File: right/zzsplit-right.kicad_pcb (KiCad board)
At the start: 2 copper layers, 160.9 x 98.9 mm, 77 parts, among them J1 OLED, J2 MJ-4PP-9-Lily58-cache, J3 OLED, SW1 SW_PUSH-MX_W_LED, SW10 SW_PUSH-MX_W_LED, SW11 SW_PUSH-MX_W_LED, SW12 SW_PUSH-MX_W_LED, SW13 SW_PUSH-MX_W_LED, SW14 SW_PUSH-MX_W_LED, SW15 SW_PUSH-MX_W_LED, SW16 SW_PUSH-MX_W_LED, SW17 SW_PUSH-MX_W_LED, SW18 SW_PUSH-MX_W_LED, SW19 SW_PUSH-MX_W_LED, SW2 SW_PUSH-MX_W_LED, SW20 SW_PUSH-MX_W_LED, SW21 SW_PUSH-MX_W_LED, SW22 SW_PUSH-MX_W_LED, SW23 SW_PUSH-MX_W_LED, SW24 SW_PUSH-MX_W_LED, SW25 SW_PUSH-MX_W_LED, SW26 SW_PUSH-MX_W_LED, SW27 SW_PUSH-MX_W_LED, SW28 SW_PUSH-MX_W_LED, SW29 SW_PUSH-MX_W_LED, SW3 SW_PUSH-MX_W_LED, SW30 SW_PUSH-MX_W_LED, SW31 SW_SPDT, SW32 SW_Push, SW4 SW_PUSH-MX_W_LED, SW5 SW_PUSH-MX_W_LED, SW6 SW_PUSH-MX_W_LED, SW7 SW_PUSH-MX_W_LED, SW8 SW_PUSH-MX_W_LED, SW9 SW_PUSH-MX_W_LED, U1 ProMicro

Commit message: pcb fixup && new gerber
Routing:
- net GND: track 198.5 -> 209.7 mm, vias 42 -> 52
- net VDD: track 1395.2 -> 1401.0 mm
- net Net-(SW16-Pad3): track 45.3 -> 43.9 mm
- net Col4: track 180.0 -> 181.1 mm

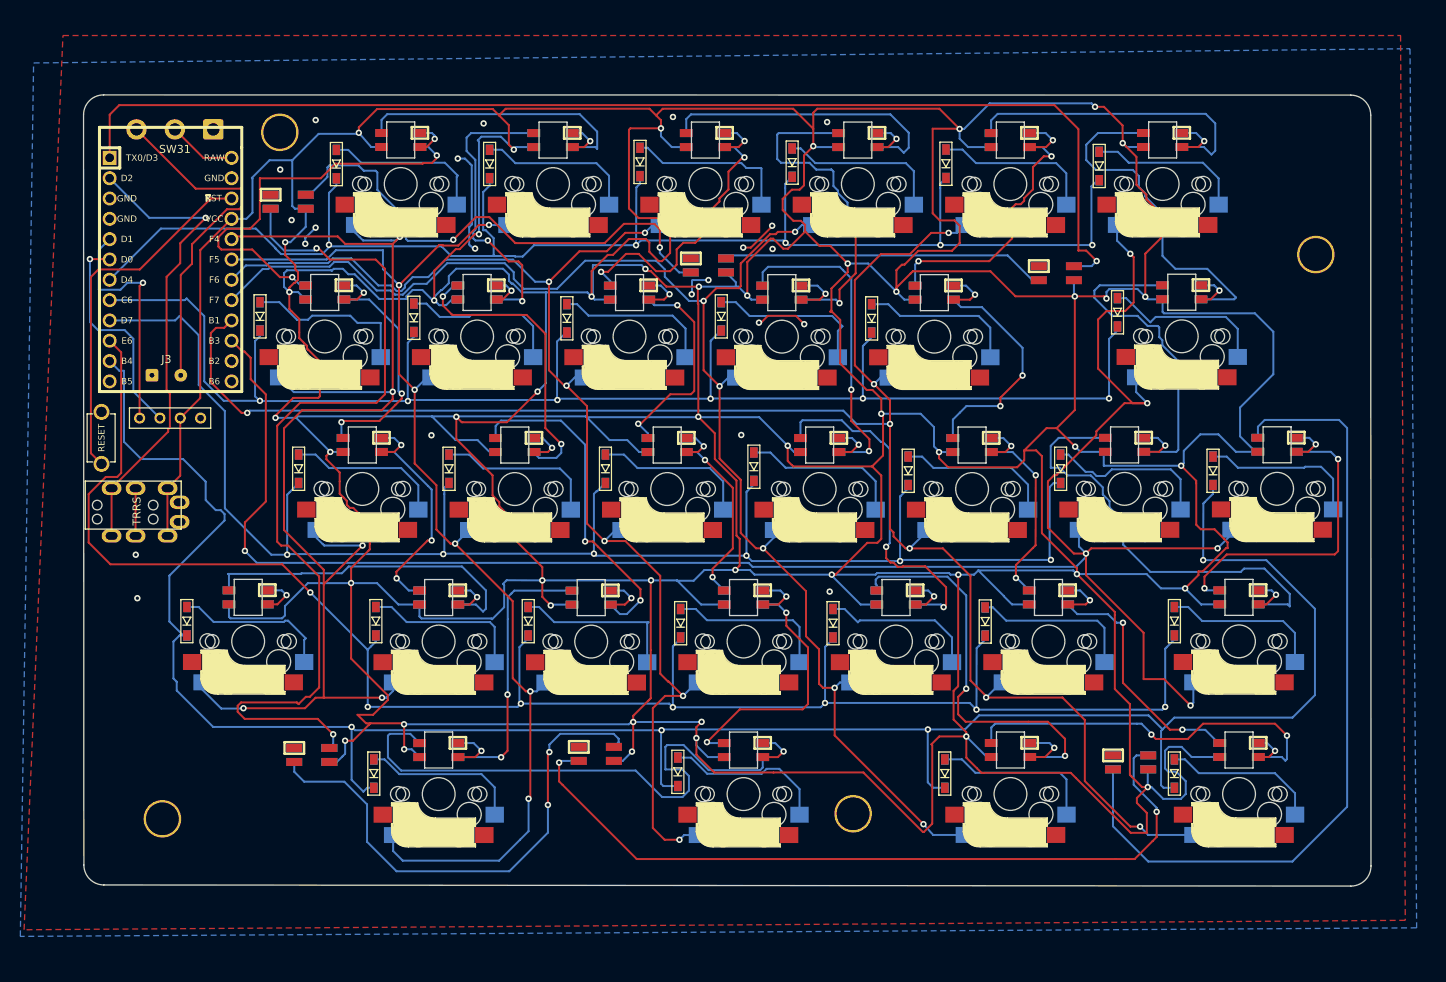
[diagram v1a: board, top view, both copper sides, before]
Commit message: fix rgb powerline problem and new 3 pin 2 channel switches
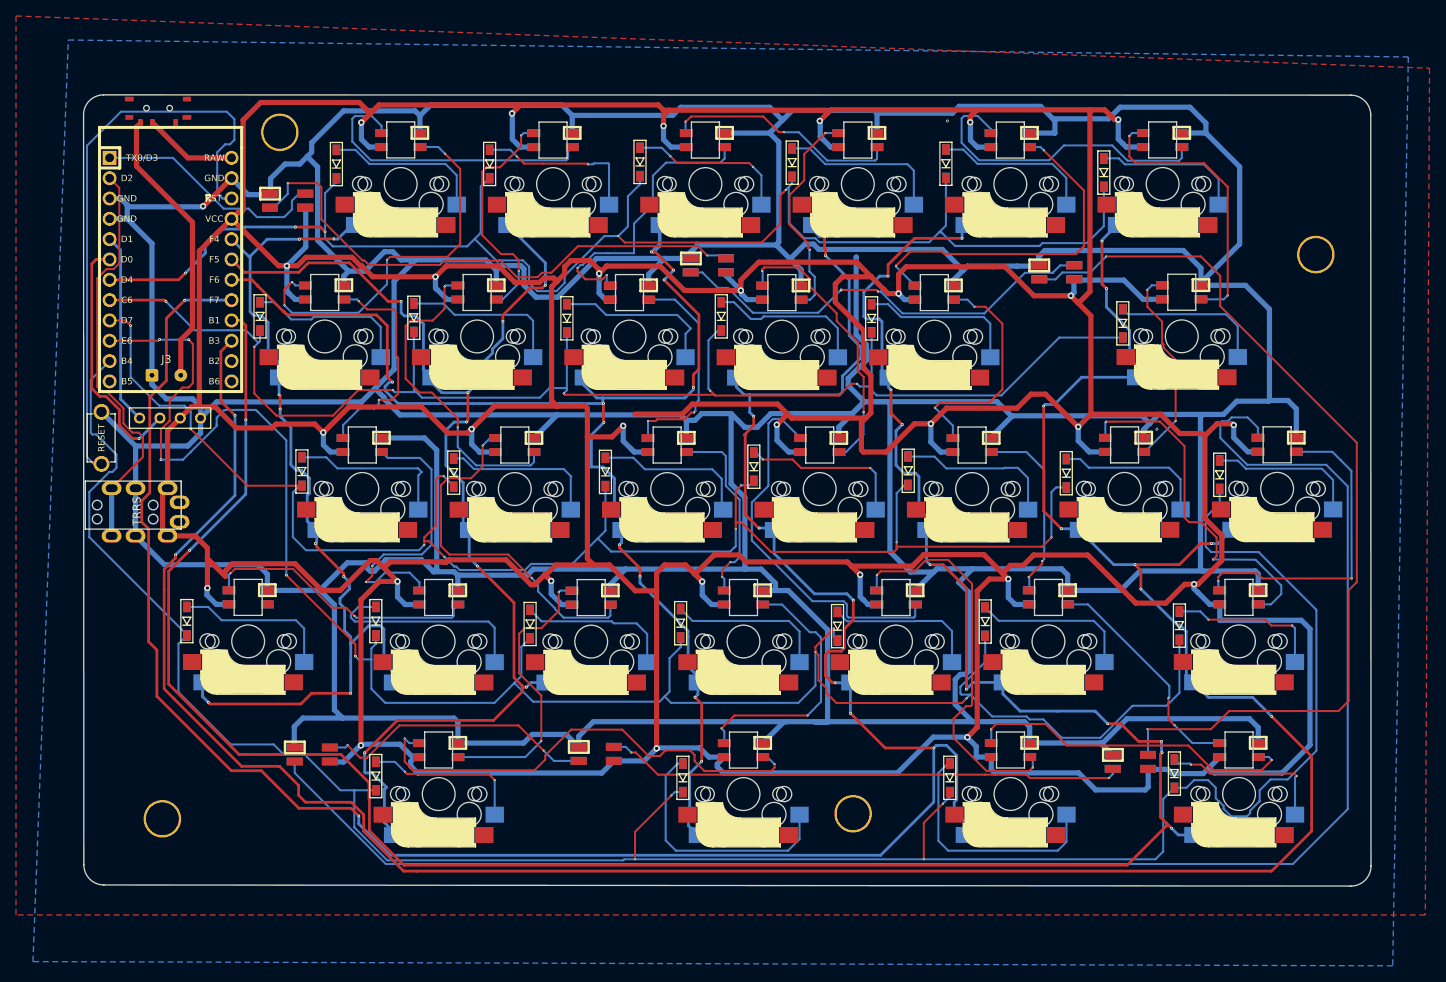
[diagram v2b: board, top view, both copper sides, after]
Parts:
- J3: value OLED -> Conn_01x02_Female
- SW31: footprint Connector_Wire:SolderWire-0.75sqmm_1x03_P4.8mm_D1.25mm_OD2.3mm -> switch:switch-MSK-12C02-smd
- moved D34 102.3 mm to (218.8, 130.4)
- moved D36 102.3 mm to (116.5, 129.4)
- moved D31 96.5 mm to (113.4, 60.2)
- moved D33 96.5 mm to (209.6, 69.2)
- moved SW31 7.98 mm to (97.2, 47.3), turned to -90 degrees
- moved D27 1.53 mm to (217.8, 75.5)
- moved D26 1.00 mm to (215.5, 56.7)
- moved D15 0.98 mm to (162.8, 132.4)
- moved D30 0.97 mm to (229.9, 94.5)
- moved D28 0.90 mm to (210.8, 94.3)
- moved D29 0.84 mm to (224.9, 113.3)
- moved D20 0.82 mm to (196.2, 132.4)
- moved D8 0.76 mm to (134.2, 94.2)
- moved D19 0.67 mm to (182.2, 113.4)
- moved D3 0.54 mm to (115.2, 94.1)
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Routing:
- net GND: track 209.7 -> 1098.1 mm, vias 52 -> 3
- net VDD: track 1401.0 -> 1122.2 mm, vias 48 -> 29
- net LED: track 149.3 -> 29.4 mm, vias 1 -> 0
- net Col4: track 181.1 -> 294.4 mm, vias 6 -> 10
- net backlight: track 101.7 -> 208.1 mm
- net Col5: track 221.0 -> 310.2 mm, vias 7 -> 12
- net Col6: track 250.7 -> 327.2 mm, vias 6 -> 10
- net Net-(D35-Pad1): track 97.7 -> 35.4 mm
- net Col1: track 156.0 -> 114.0 mm, vias 5 -> 8
- net Reset: track 45.6 -> 74.2 mm
- net Net-(D31-Pad1): track 40.5 -> 68.9 mm, vias 0 -> 2
- net Row4: track 225.0 -> 243.3 mm, vias 7 -> 8
- net Net-(SW10-Pad1): track 42.3 -> 27.1 mm
- net Net-(SW12-Pad3): track 40.0 -> 25.7 mm, vias 0 -> 2
- net Row2: track 189.8 -> 177.3 mm
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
